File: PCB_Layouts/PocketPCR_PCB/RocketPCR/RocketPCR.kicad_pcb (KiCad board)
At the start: 2 copper layers, 105 x 33 mm, 50 parts, among them J1 Conn_01x02_Male, J2 Conn_02x05_Odd_Even, J3 USB_C_Receptacle, Q1 Q_NMOS_GSD, Q2 Q_NMOS_GSD, Q3 Q_NMOS_GSD, SW1 Rotary_Encoder_Switch, U1 TLV1117-33, U2 SAMD21G18B-A changed from SAM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, X1 PAD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

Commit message: New Version with Bottom Heater Improved software
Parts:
- removed D1: DIODE, Diode_SMD:D_1210_3225Metric
- removed L1: L, Inductor_SMD:L_1206_3216Metric
- added C13: 100nF, Capacitor_SMD:C_0805_2012Metric, B.Cu at (121.0, 97.2)
- added R6: 4.7k, Resistor_SMD:R_0805_2012Metric, B.Cu at (128.2, 94.6)
- added X12: PAD, GaudiLabsFootPrints:SolderPad1_8mm, B.Cu at (83.2, 98.5)
- added X13: PAD, GaudiLabsFootPrints:SolderPad1_8mm, B.Cu at (83.3, 101.1)
- C3: footprint Capacitor_SMD:C_1206_3216Metric -> GaudiLabsFootPrints:C_2512_HandSoldering
- J3: footprint Connectors_USB:USB_C_Receptacle_Amphenol_12401610E4-2A -> GaudiLabsFootPrints:USB_C_Receptacle_Amphenol_12401610E4-2A
- R4: value 390k -> 4.7k
- moved C3 3.57 mm to (166.1, 111.8)
- moved X5 2.20 mm to (83.3, 95.8)
- moved X1 2.00 mm to (83.3, 104.0)
- moved C16 1.53 mm to (127.8, 110.4)
- moved C14 1.41 mm to (127.8, 106.3)
- moved Q2 0.73 mm to (121.3, 105.0)
- moved Q3 0.50 mm to (118.0, 100.2)
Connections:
- C3 pad 1: Net-(C3-Pad1) -> V_USB
- J1 pad 2: Net-(C3-Pad1) -> V_USB
- U2 pad 7: (no net) -> TEMP_LID
- X1 pad 1: Net-(C3-Pad1) -> V_USB
- X4 pad 1: Net-(C3-Pad1) -> V_USB
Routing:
- net Net-(C3-Pad1): track 126.5 -> 0.00 mm, vias 4 -> 0
- net V_USB: track 132.2 -> 257.8 mm, vias 0 -> 4
- net TEMP_LID: track 0.00 -> 104.3 mm, vias 0 -> 5
- net +3V3: track 138.0 -> 179.6 mm, vias 6 -> 7
- net GND: track 111.8 -> 115.4 mm, vias 9 -> 11
- net Net-(Q3-Pad3): track 62.5 -> 60.5 mm
- net Net-(C16-Pad1): track 11.6 -> 13.2 mm
- net Net-(C16-Pad2): track 13.1 -> 14.7 mm
- net Net-(C14-Pad1): track 7.48 -> 9.01 mm
- net Net-(C14-Pad2): track 9.55 -> 11.0 mm
- net ENC2: track 51.7 -> 50.6 mm
- net Net-(J1-Pad1): track 8.32 -> 7.50 mm
- net DISP_SDA: track 15.3 -> 15.9 mm
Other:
- outline, holes or cut-outs redrawn
- board text added: "+"
- board text added: "Pocket PCR V1.1, 2019, gaudi.ch"
- board text removed: "Pocket PCR V1.0, 2019, gaudi.ch"

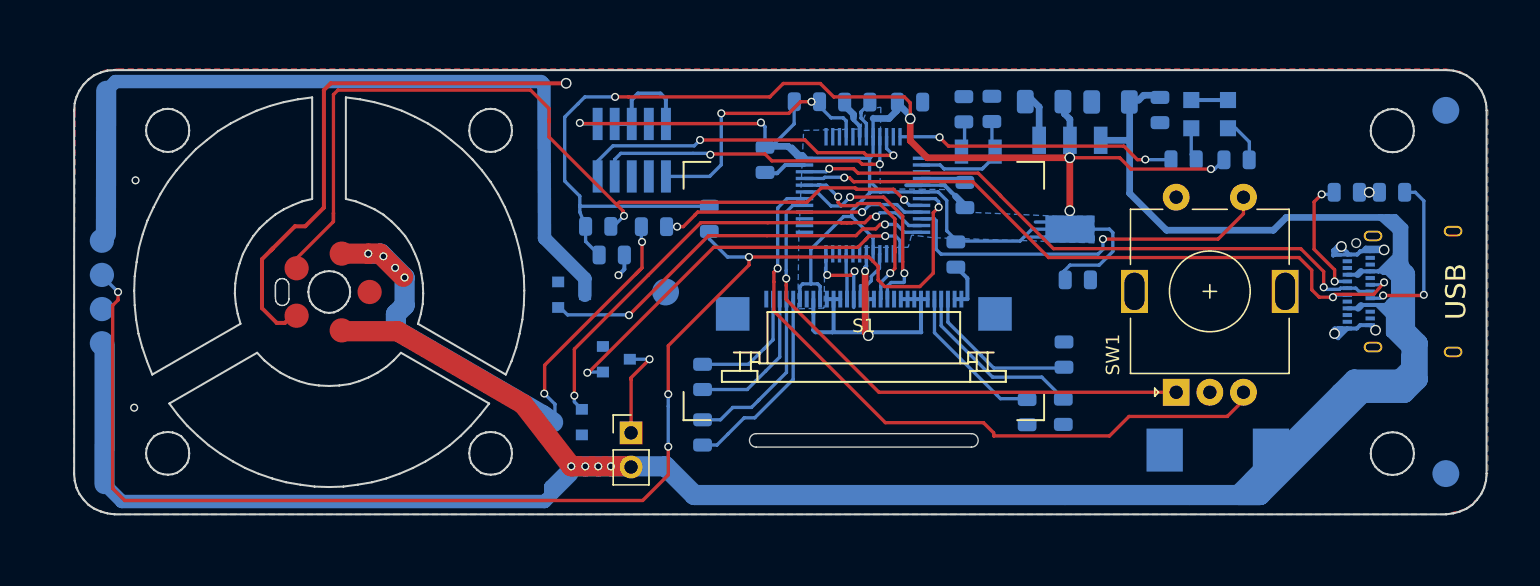
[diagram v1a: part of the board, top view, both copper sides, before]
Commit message: Updated PCB, BOM, added Heater Hardware
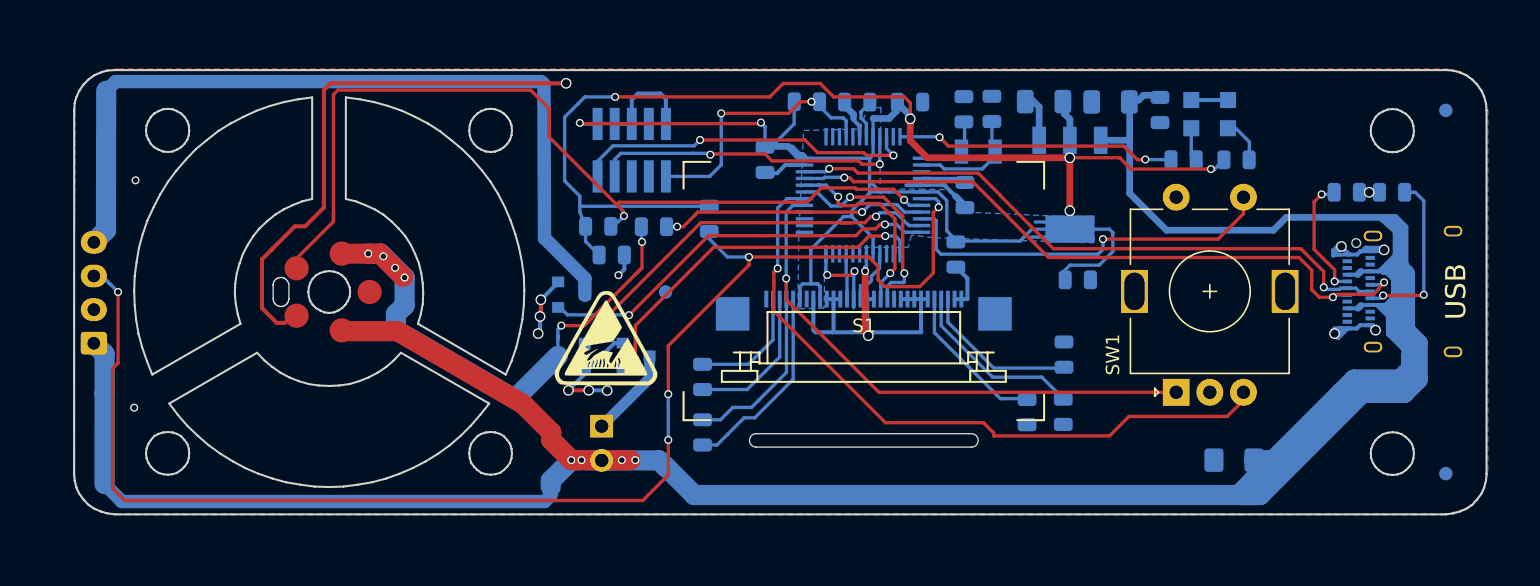
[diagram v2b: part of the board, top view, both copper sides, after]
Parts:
- removed X1, X12, X13, X5: PAD, GaudiLabsFootPrints:SolderPad1_8mm
- added G***: LOGO, GaudiLabsLogos:HotSurfaceWarning, F.Cu at (120.6, 103.5)
- added J4: Conn_01x04_Female, Connector_JST:JST_XH_S04B-XH-A_1x04_P2.50mm_Horizontal, B.Cu at (82.5, 103.8)
- C3: footprint GaudiLabsFootPrints:C_2512_HandSoldering -> Capacitor_SMD:C_1206_3216Metric_Pad1.42x1.75mm_HandSolder
- J1: footprint Connector_PinHeader_2.54mm:PinHeader_1x02_P2.54mm_Vertical -> GaudiLabsFootPrints:PinHeader_JST_1x02_P2.54mm_Vertical; moved to B.Cu
- R5: value 100k -> 390k
- X10, X11, X9: footprint GaudiLabsFootPrints:Fiducial_Cooper -> GaudiLabsFootPrints:Fiducial_1mm_Dia_2.54mm_Outer_CopperBottom
- moved Q1 4.93 mm to (118.0, 104.8)
- moved J1 2.32 mm to (120.2, 111.2), turned to 180 degrees
- moved Q2 1.48 mm to (122.8, 104.8)
- moved C3 1.42 mm to (167.2, 112.5)
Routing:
- net GND: track 115.4 -> 128.7 mm, vias 11 -> 17
- net BLOCK: track 35.9 -> 30.7 mm
- net VSENS: track 45.2 -> 42.5 mm
- net FAN: track 30.0 -> 27.5 mm
- net TEMP_LID: track 104.3 -> 105.8 mm
- net Net-(J4-Pad4): track 60.5 -> 61.5 mm
- net Net-(J1-Pad1): track 7.50 -> 7.20 mm, vias 1 -> 0
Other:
- outline, holes or cut-outs redrawn
- board text added: "Pocket PCR V1.2, 2020, gaudi.ch"
- board text removed: "Pocket PCR V1.1, 2019, gaudi.ch"
